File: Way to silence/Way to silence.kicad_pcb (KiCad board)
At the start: 2 copper layers, 59.3 x 38.1 mm, 68 parts, among them J1 SD Card Connector, J2 Amplificator_Terminal, J3 5V_Terminal, J4 Battery_Terminal, J5 LEDS Port, Q1 BC817, Q2 BC817, SW1 SW_SPDT, SW3 SW_SPST, U1 ESP32-WROOM-32-N16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

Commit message: [DRC] No warnings, no errors
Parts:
- removed G***, IMAGE: LOGO, LOGO
- added REF**: way_to_silence_illustration, Way to silence:way_to_silence_illustration, F.Cu at (98.3, 77.6)
- added REF**: juthomas_fr_qrcode, Way to silence:juthomas_fr_qrcode, F.Cu at (76.8, 76.2)

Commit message: [UDPT] Pcb from schematics
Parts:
- added C21: 10uF, Way to silence:C_0603_1608Metric, F.Cu at (73.3, 73.2)
- added R21: 10K, Way to silence:R_0603_1608Metric, F.Cu at (76.1, 73.2)
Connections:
- J1 pad 2: unconnected-(J1-DAT3/CD-Pad2) -> /ESP_IO5
- J1 pad 3: /ESP_IO5 -> /ESP_IO23
- J1 pad 8: /ESP_IO23 -> unconnected-(J1-DAT1-Pad8)
- R2 pad 2: /ESP_IO18 -> /ESP_IO23
- R3 pad 2: /ESP_IO19 -> /ESP_IO18
- R4 pad 2: /ESP_IO23 -> /ESP_IO19
- SW3 pad 1: /ESP_IO0 -> /ESP_EN
- U3 pad 25: /ESP_RX -> /ESP_TX
- U3 pad 26: /ESP_TX -> /ESP_RX
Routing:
- net /ESP_EN: track 24.4 -> 57.4 mm, vias 0 -> 2
- net +3.3V: track 84.2 -> 99.5 mm, vias 8 -> 9
- net /ESP_IO0: track 28.7 -> 23.5 mm
- net /ESP_IO18: track 34.1 -> 29.9 mm, vias 3 -> 2
- net /ESP_IO23: track 19.4 -> 15.5 mm
- net /ESP_IO19: track 29.5 -> 26.1 mm, vias 3 -> 2
- net GND: track 74.8 -> 76.0 mm
- net /ESP_RX: track 35.1 -> 36.0 mm
- net unconnected-(J1-DAT1-Pad8): track 0.00 -> 0.64 mm

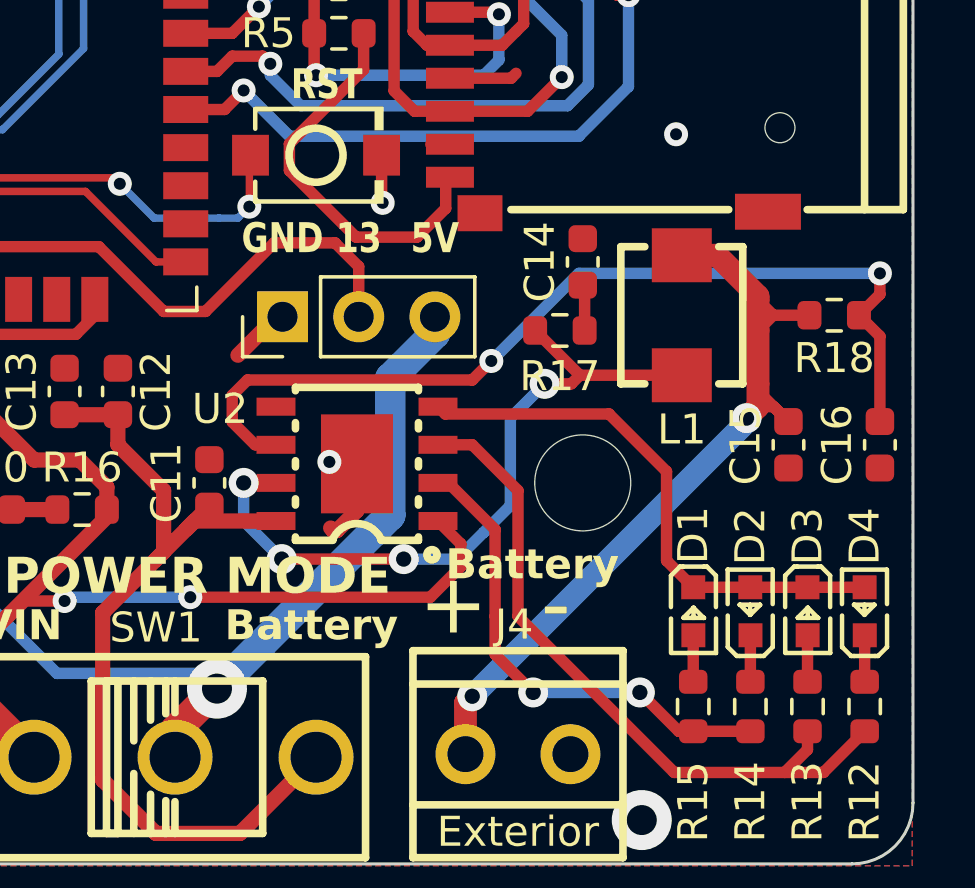
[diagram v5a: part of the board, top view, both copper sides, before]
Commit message: [ADD] IO port
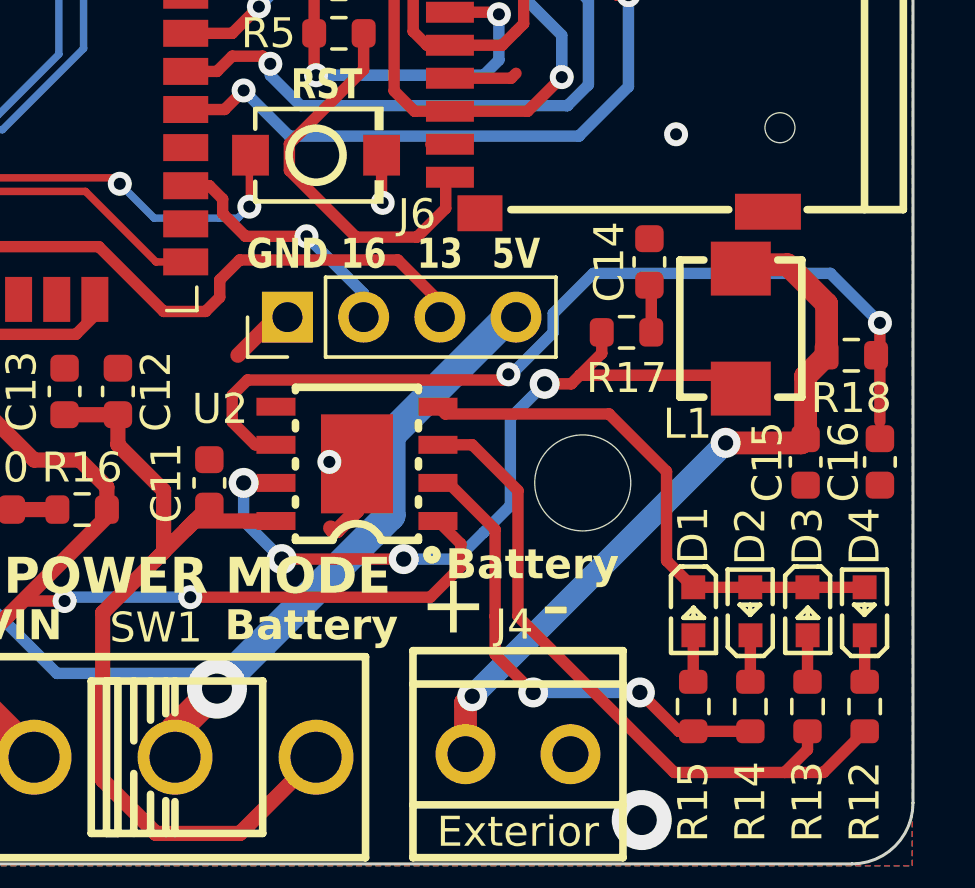
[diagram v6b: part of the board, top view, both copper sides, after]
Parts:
- removed J5: LEDS Port, Way to silence:PinHeader_1x03_P2.54mm_Vertical
- added J6: Conn_01x04_Pin, Way to silence:PinHeader_1x04_P2.54mm_Vertical, F.Cu at (112.9, 71.4)
- moved R17 2.22 mm to (120.4, 71.9)
- moved C14 2.22 mm to (121.2, 69.5)
- moved L1 2.02 mm to (124.2, 71.8)
- moved R18 1.45 mm to (127.9, 72.6)
- moved C15 0.81 mm to (126.4, 76.2)
- moved C16 0.57 mm to (128.8, 76.2)
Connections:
- U1 pad 27: unconnected-(U1-IO16-Pad27) -> /ESP_IO16
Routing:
- net /ESP_IO16: track 0.00 -> 8.49 mm, vias 0 -> 1
- net /BMS/BAT: track 28.0 -> 25.0 mm
- net /ESP_IO13: track 24.2 -> 26.1 mm
- net Net-(U2-SW): track 23.8 -> 25.7 mm
- net +5V: track 85.4 -> 86.7 mm
- net Net-(U2-BAT): track 31.5 -> 30.3 mm

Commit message: [UDPT] Pcb from schematics
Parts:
- removed C13, C15: 22uF, Way to silence:C_0603_1608Metric
- removed C14: 4.7nF, Way to silence:C_0603_1608Metric
- removed R18: 0.1R, Way to silence:R_0603_1608Metric
- added SW2: SW_SPST, Way to silence:SW_SPST, F.Cu at (113.7, 76.3)
- C12: value 22uF -> 10uF
- L1: value 1UH -> 2.2UH; footprint Way to silence:Inductor -> Way to silence:Inductor-0630LR
- R16: value 0.5R -> 1R
- R17: value 1R -> 10K
- moved C16 19.3 mm to (109.6, 77.7), turned to 180 degrees
- moved R17 11.0 mm to (113.0, 80.0), turned to 180 degrees
- moved U2 7.78 mm to (103.6, 76.5), turned to 0 degrees
- moved C12 6.41 mm to (109.6, 75.6), turned to 0 degrees
- moved R16 6.18 mm to (97.5, 73.8), turned to 0 degrees
- moved C11 4.22 mm to (109.6, 74.0), turned to 0 degrees
- moved C9 4.08 mm to (97.5, 77.9), turned to 180 degrees
- moved C10 2.95 mm to (97.5, 75.3)
- moved L1 2.62 mm to (126.2, 73.4)
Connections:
- C10 pad 1: Net-(C10-Pad1) -> /USB to Uart/+5V
- C10 pad 2: GND -> Net-(C10-Pad2)
- C16 pad 2: Net-(U2-BAT) -> /BMS/BAT
- R16 pad 1: /USB to Uart/+5V -> Net-(C10-Pad2)
- R16 pad 2: Net-(C10-Pad1) -> GND
- R17 pad 1: Net-(U2-SW) -> Net-(SW2-B)
- R17 pad 2: Net-(C14-Pad1) -> Net-(U2-KEY)
- U2 pad 5: unconnected-(U2-KEY-Pad5) -> Net-(U2-KEY)
- U2 pad 6: Net-(U2-BAT) -> /BMS/BAT
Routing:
- net Net-(U2-BAT): track 30.3 -> 0.00 mm, vias 2 -> 0
- net /USB to Uart/+5V: track 90.6 -> 70.5 mm, vias 4 -> 2
- net Net-(U2-LED1): track 16.3 -> 32.0 mm
- net Net-(U2-LED2): track 23.5 -> 36.4 mm, vias 0 -> 2
- net /BMS/BAT: track 25.0 -> 37.5 mm, vias 2 -> 0
- net Net-(D1-K): track 18.5 -> 29.5 mm, vias 0 -> 2
- net GND: track 76.0 -> 84.9 mm
- net Net-(U2-KEY): track 0.00 -> 6.56 mm, vias 0 -> 2
- net Net-(U2-SW): track 25.7 -> 22.1 mm, vias 4 -> 2
- net Net-(SW2-B): track 0.00 -> 1.58 mm
- net Net-(C10-Pad2): track 0.00 -> 1.54 mm
- net Net-(C14-Pad1): track 1.54 -> 0.00 mm
- net Net-(C10-Pad1): track 1.53 -> 0.00 mm
- net /BMS/VOUT: track 29.9 -> 31.2 mm, vias 0 -> 2
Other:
- outline, holes or cut-outs redrawn
